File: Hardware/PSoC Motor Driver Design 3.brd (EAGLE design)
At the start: 20.3 x 35.6 mm, 47 parts, among them J1 DNP, J2 DNP, J4 DNP, J5 DNP, J6 DNP, J7 DNP, J8 CORTEX_DEBUGPTH, U1 CY8C4245LQI-483, U2 DRV8835

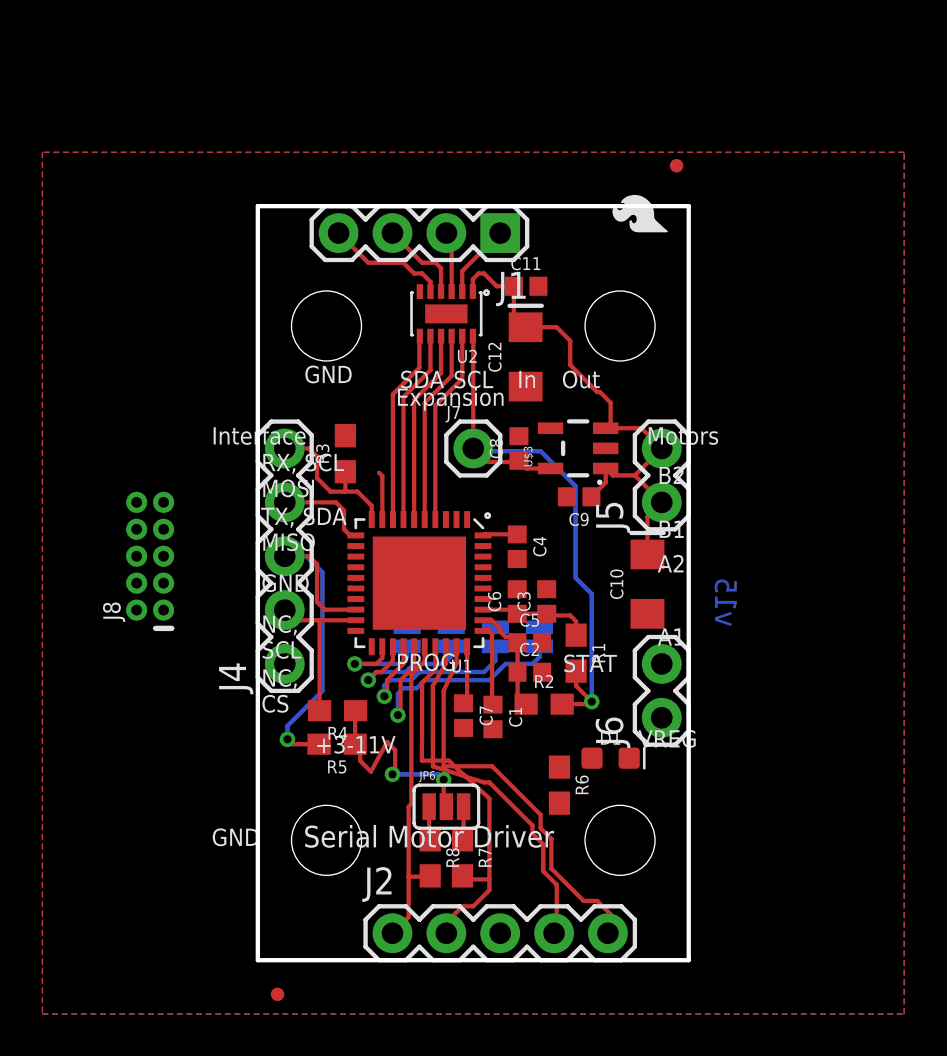
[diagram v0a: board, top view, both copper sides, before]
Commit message: Fixed schematic naming, touched up other changes, tested 2nd serial port, reved board number
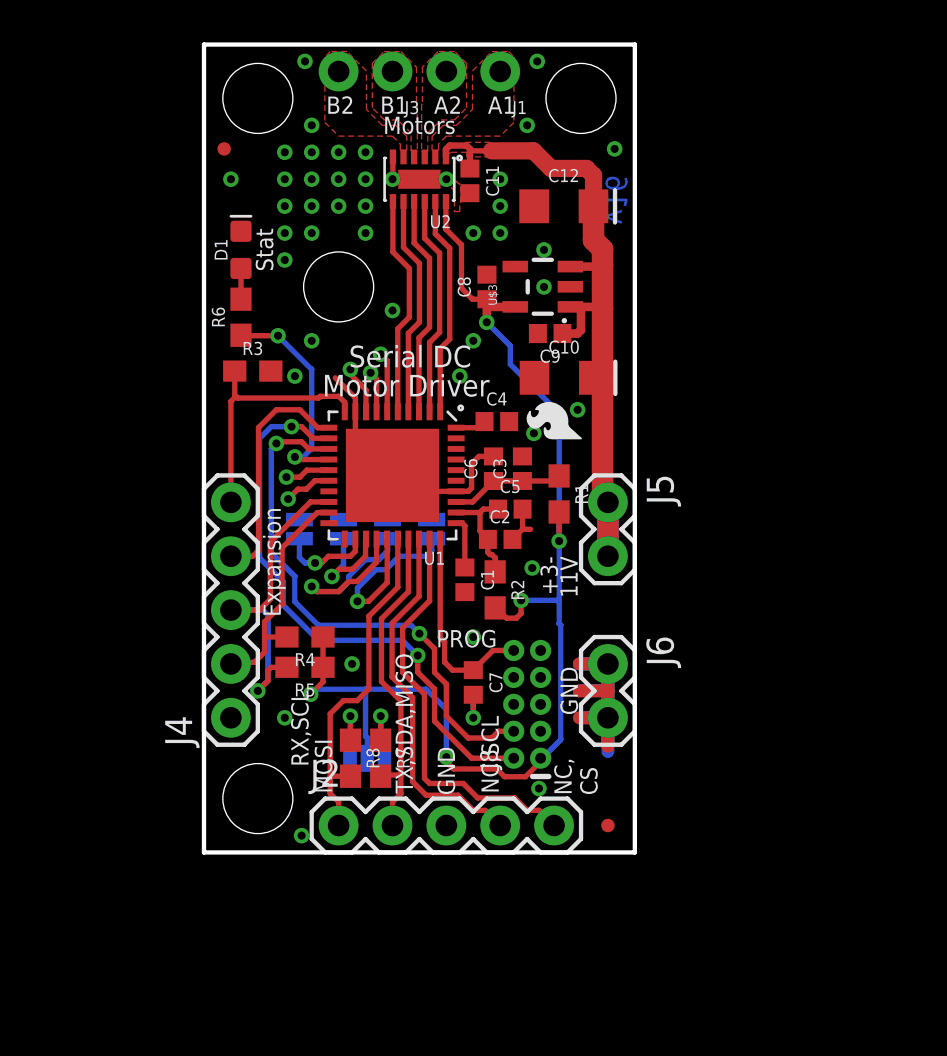
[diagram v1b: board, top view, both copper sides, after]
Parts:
- removed J7: DNP, SparkFun-Connectors:1X01
- removed U$1: (no value), SparkFun-Actobotics:ACTOBOTICS_CHANNEL_SINGLE_DRILL_REF
- added J3: DNP, SparkFun-Connectors:1X02_NO_SILK
- J1: device SparkFun-Connectors:1X04 -> SparkFun-Connectors:1X02_NO_SILK
- J5, J6: device SparkFun-Connectors:1X02 -> SparkFun-Connectors:1X02@1
- R4, R5: value 4.7k -> 10k
- moved D1 29.6 mm to (1.75, 28.4), turned to 90 degrees
- moved H1 29.3 mm to (6.35, 26.7)
- moved R6 26.7 mm to (1.75, 25.2), turned to 90 degrees
- moved LOGO2 22.6 mm to (5.24, 10.2), turned to 90 degrees
- moved LOGO3 22.3 mm to (11.3, 5.91), turned to 90 degrees
- moved FD2 21.4 mm to (0.95, 33.2)
- moved J8 19.1 mm to (15.2, 6.99)
- moved FD1 17.5 mm to (19.1, 1.27)
- moved H2 11.2 mm to (2.54, 35.6)
- moved H3 10.9 mm to (17.8, 35.6)
- moved LOGO1 10.6 mm to (18.1, 19.2)
- moved C10 10.5 mm to (17.0, 22.4), turned to 0 degrees
- moved FRAME1 9.67 mm to (-21.6, -27.9)
- moved C9 7.82 mm to (16.3, 24.5)
- moved U$3 7.80 mm to (16.0, 26.7)
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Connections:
- net N$5 renamed AOUT1
- net N$6 renamed AOUT2
- net P3.5_US renamed U3.5
- removed net N$7: J1.3, U2.4
- removed net N$8: J1.4, U2.5
- removed net P2.5: U1.6, U2.9
- removed net P2.6: U1.7, U2.8
- removed net P2.7: U1.8, U2.7
- removed net P3.4_US: U1.14
- new net BOUT1: J3.1, U2.4
- new net BOUT2: J3.2, U2.5
- new net P2.1: U1.2, U2.10
- new net P2.2: U1.3, U2.9
- new net SLED: R6.1, U1.14
- new net U2.5: U1.6
- new net U2.6: U1.7
- new net U2.7: U1.8
- new net U3.6: U1.16
- net P2.0: now also U2.11; no longer R6.1
- net P2.3: now also U2.8; no longer U2.11
- net P2.4: now also U2.7; no longer U2.10
- net VCC: no longer J7.1
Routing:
- net GND: track 2.27 -> 31.4 mm, vias 0 -> 44
- net P3.2: track 0.00 -> 27.3 mm, vias 0 -> 2
- net P3.3: track 0.00 -> 25.3 mm, vias 0 -> 2
- net VCC: track 39.0 -> 58.5 mm, vias 3 -> 5
- net P2.2: track 0.00 -> 10.4 mm
- net P2.1: track 0.00 -> 10.4 mm
- net P2.0: track 0.00 -> 10.4 mm
- net SLED: track 0.00 -> 10.3 mm, vias 0 -> 2
- net VIN: track 25.0 -> 35.3 mm
- net P2.7: track 9.18 -> 0.00 mm
- net P2.6: track 9.18 -> 0.00 mm
- net P2.5: track 9.18 -> 0.00 mm
- net !RESET: track 2.74 -> 9.69 mm
- net CONFIG_OUT: track 4.52 -> 11.2 mm
- net N$8: track 5.74 -> 0.00 mm
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- added copper zone on layer 1, net AOUT1
- added copper zone on layer 1, net AOUT2
- added copper zone on layer 1, net BOUT1
- added copper zone on layer 1, net BOUT2
- added copper zone on layer 1, net VIN
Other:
- board size 20.3 x 35.6 mm -> 20.3 x 38.1 mm
- board text added: "(Open=UART)"
- board text added: "+3- 11V"
- board text added: "A"
- board text added: "B"
- board text added: "MOSI"
- board text added: "NC,SCL"
- board text added: "REG OUT"
- board text added: "RX,SCL"
- board text added: "Serial DC Motor Driver"
- board text added: "Stat"
- board text added: "TX,SDA,MISO"
- board text added: "These lines depict the width of typical TO-220 heatsinks."
- board text added: "v16"
- board text removed: "(bridge='1')"
- board text removed: "+"
- board text removed: "0000:UART 0001:SPI 0010:SLV 0011:0x58 0100:0x59 (...)"
- board text removed: "Interface"
- board text removed: "NC, SCL"
- board text removed: "RX, SCL MOSI"
- board text removed: "STAT"
- board text removed: "Serial Motor Driver"
- board text removed: "TX, SDA MISO"
- board text removed: "VREG"
- board text removed: "v15"
